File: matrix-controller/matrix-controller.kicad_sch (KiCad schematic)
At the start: 1 part

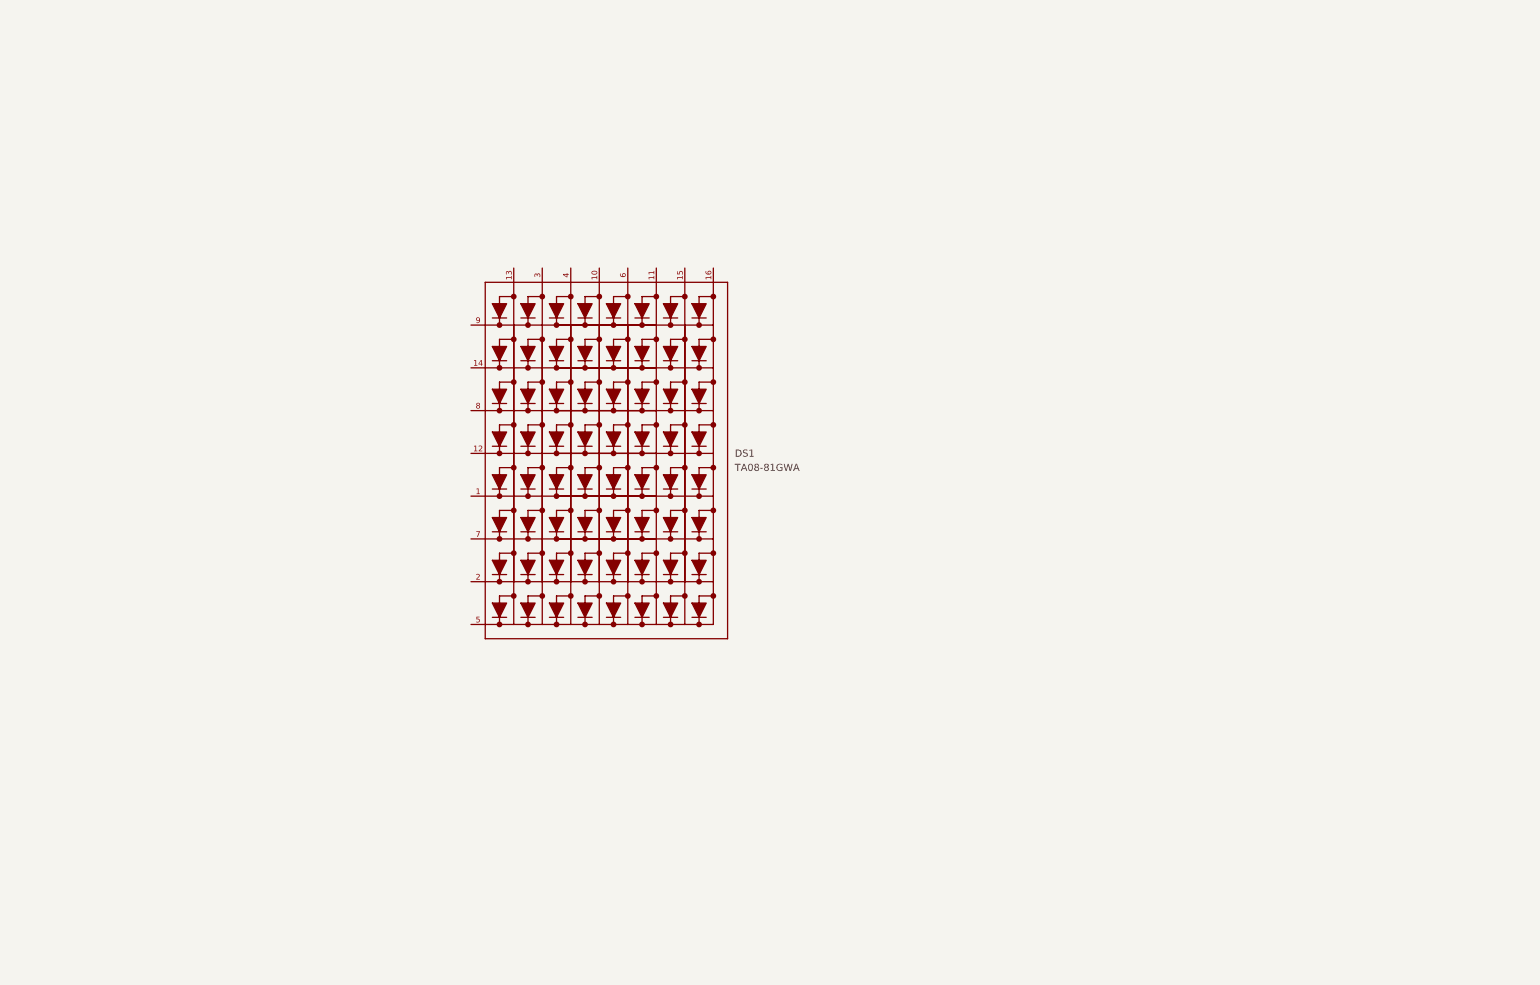
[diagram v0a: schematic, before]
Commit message: Base of the schematic is done, need to add IMU and regulator and finish the rest of the panels
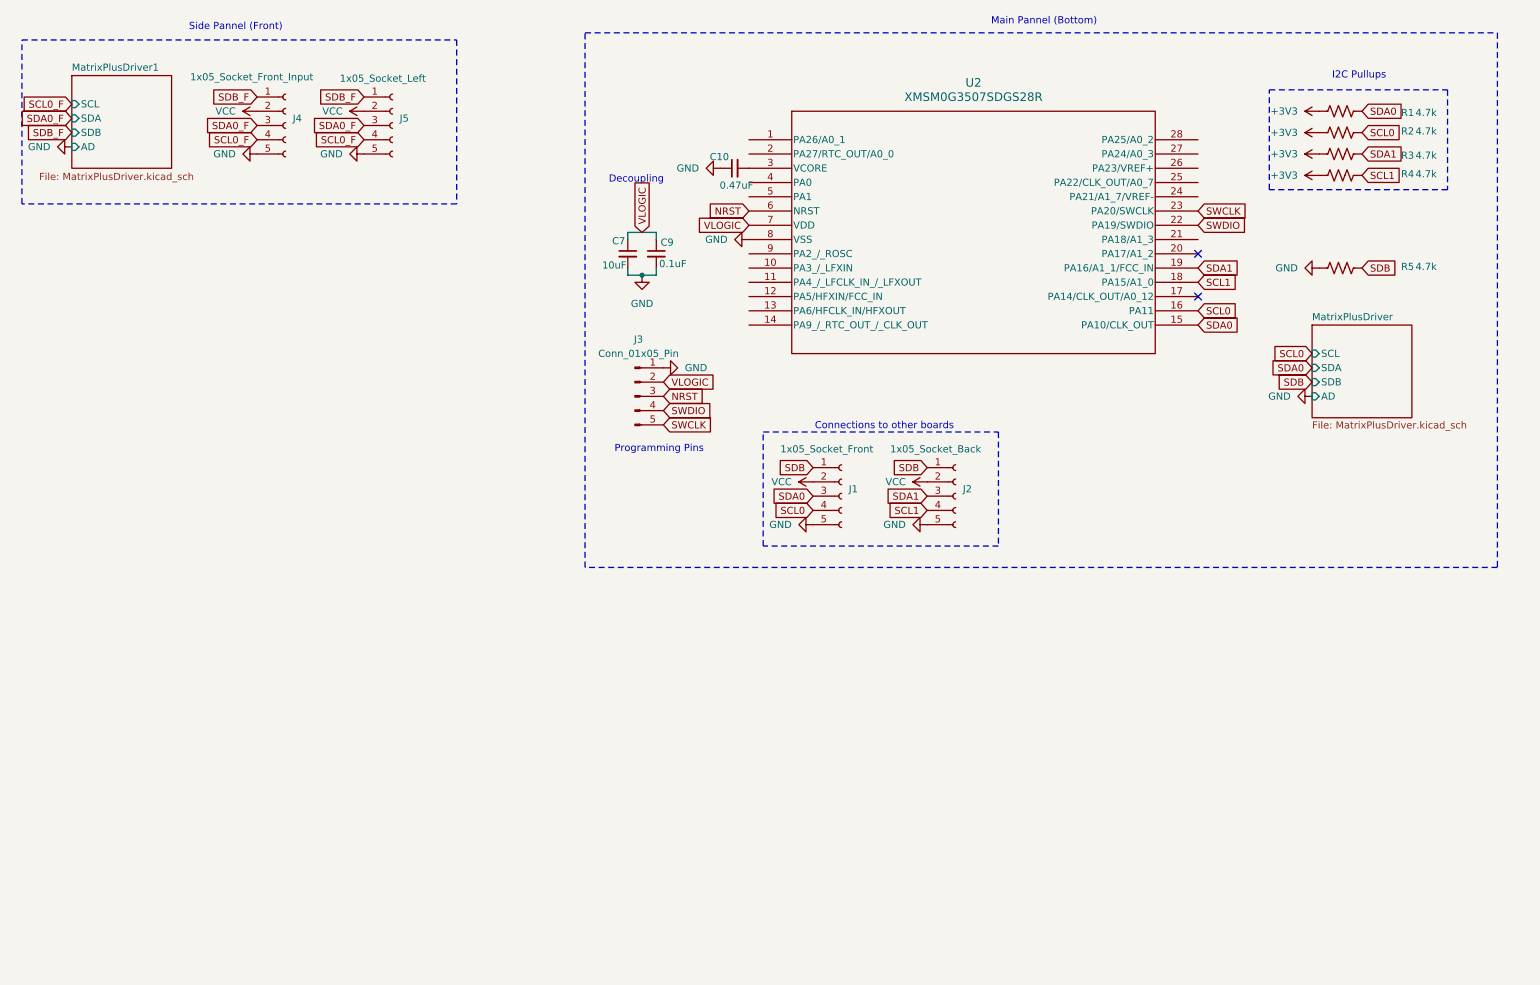
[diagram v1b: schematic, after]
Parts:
- removed DS1: TA08-81GWA, TA08-81GWA:DISPLAY_TA08-81GWA, symbol TA08-81GWA:TA08-81GWA
- added C10: 0.47uF, Capacitor_SMD:C_1206_3216Metric, symbol Device:C_Small
- added C7: 10uF, Capacitor_SMD:C_1206_3216Metric, symbol Device:C_Small
- added C9: 0.1uF, Capacitor_SMD:C_1206_3216Metric, symbol Device:C_Small
- added J1: 1x05_Socket_Front, Connector_PinSocket_2.00mm:PinSocket_1x05_P2.00mm_Vertical, symbol Connector:Conn_01x05_Socket
- added J2: 1x05_Socket_Back, Connector_PinSocket_2.00mm:PinSocket_1x05_P2.00mm_Vertical, symbol Connector:Conn_01x05_Socket
- added J3: Conn_01x05_Pin, Connector_PinSocket_2.54mm:PinSocket_1x05_P2.54mm_Vertical, symbol Connector:Conn_01x05_Pin
- added J4: 1x05_Socket_Front_Input, Connector_PinSocket_2.00mm:PinSocket_1x05_P2.00mm_Vertical, symbol Connector:Conn_01x05_Socket
- added J5: 1x05_Socket_Left, Connector_PinSocket_2.00mm:PinSocket_1x05_P2.00mm_Vertical, symbol Connector:Conn_01x05_Socket
- added R1, R2, R3, R4, R5: 4.7k, symbol Device:R_US
- added U2: XMSM0G3507SDGS28R, footprints:VSSOP28_DGS_TEX, symbol 2025-11-23_22-36-31:XMSM0G3507SDGS28R
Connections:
- new net: C10.2, U2.3 (VCORE)
- new net +3V3: R1.1, R2.1, R3.1, R4.1
- new net GND: C10.1, C7.2, C9.2, J1.5 (Pin_5), J2.5 (Pin_5), J3.1 (Pin_1), J4.5 (Pin_5), J5.5 (Pin_5), R5.1, U2.8 (VSS)
- new net NRST: J3.3 (Pin_3), U2.6 (NRST)
- new net SCL0: J1.4 (Pin_4), R2.2, U2.16 (PA11)
- new net SCL0_F: J4.4 (Pin_4), J5.4 (Pin_4)
- new net SCL1: J2.4 (Pin_4), R4.2, U2.18 (PA15/A1_0)
- new net SDA0: J1.3 (Pin_3), R1.2, U2.15 (PA10/CLK_OUT)
- new net SDA0_F: J4.3 (Pin_3), J5.3 (Pin_3)
- new net SDA1: J2.3 (Pin_3), R3.2, U2.19 (PA16/A1_1/FCC_IN)
- new net SDB: J1.1 (Pin_1), J2.1 (Pin_1), R5.2
- new net SDB_F: J4.1 (Pin_1), J5.1 (Pin_1)
- new net SWCLK: J3.5 (Pin_5), U2.23 (PA20/SWCLK)
- new net SWDIO: J3.4 (Pin_4), U2.22 (PA19/SWDIO)
- new net VCC: J1.2 (Pin_2), J2.2 (Pin_2), J4.2 (Pin_2), J5.2 (Pin_2)
- new net VLOGIC: C7.1, C9.1, J3.2 (Pin_2), U2.7 (VDD)
- no-connect marks 0 -> 2
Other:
- added sheet MatrixPlusDriver (MatrixPlusDriver.kicad_sch)
- added sheet MatrixPlusDriver1 (MatrixPlusDriver.kicad_sch)
- note added: "Connections to other boards"
- note added: "Decoupling"
- note added: "I2C Pullups"
- note added: "Main Pannel (Bottom)"
- note added: "Programming Pins"
- note added: "Side Pannel (Front)"

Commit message: Schematic of other pannels mostly completed
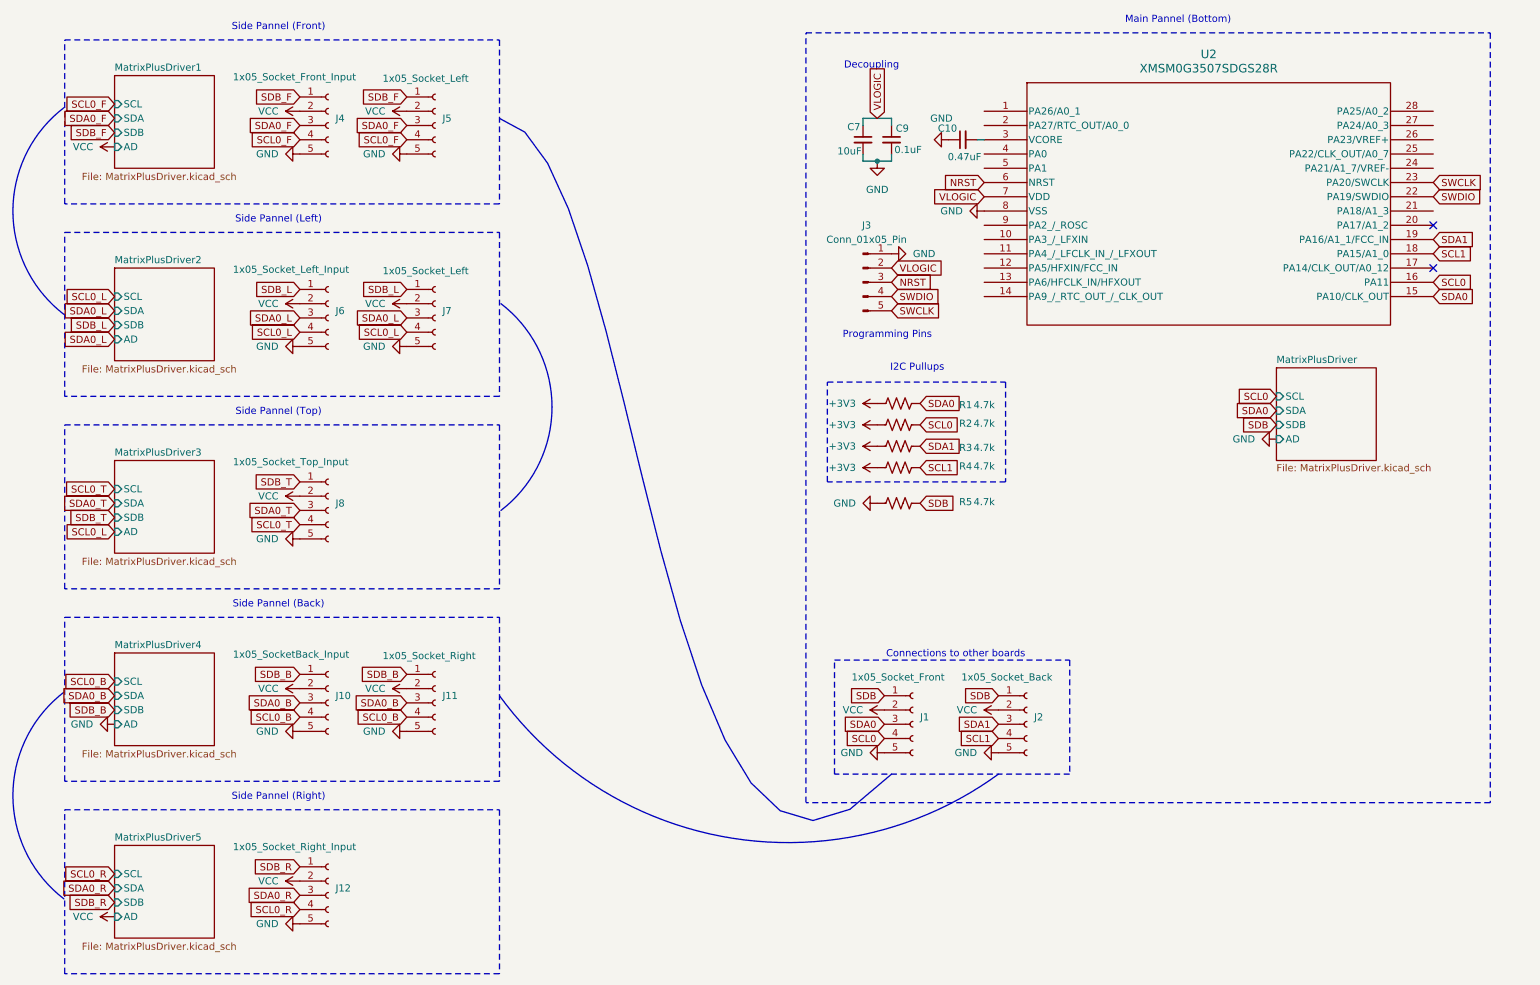
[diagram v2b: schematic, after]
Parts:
- added J10: 1x05_SocketBack_Input, Connector_PinSocket_2.00mm:PinSocket_1x05_P2.00mm_Vertical, symbol Connector:Conn_01x05_Socket
- added J11: 1x05_Socket_Right, Connector_PinSocket_2.00mm:PinSocket_1x05_P2.00mm_Vertical, symbol Connector:Conn_01x05_Socket
- added J12: 1x05_Socket_Right_Input, Connector_PinSocket_2.00mm:PinSocket_1x05_P2.00mm_Vertical, symbol Connector:Conn_01x05_Socket
- added J6: 1x05_Socket_Left_Input, Connector_PinSocket_2.00mm:PinSocket_1x05_P2.00mm_Vertical, symbol Connector:Conn_01x05_Socket
- added J7: 1x05_Socket_Left, Connector_PinSocket_2.00mm:PinSocket_1x05_P2.00mm_Vertical, symbol Connector:Conn_01x05_Socket
- added J8: 1x05_Socket_Top_Input, Connector_PinSocket_2.00mm:PinSocket_1x05_P2.00mm_Vertical, symbol Connector:Conn_01x05_Socket
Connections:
- net GND: now also J10.5 (Pin_5), J11.5 (Pin_5), J12.5 (Pin_5), J6.5 (Pin_5), J7.5 (Pin_5), J8.5 (Pin_5)
- net VCC: now also J10.2 (Pin_2), J11.2 (Pin_2), J12.2 (Pin_2), J6.2 (Pin_2), J7.2 (Pin_2), J8.2 (Pin_2)
- new net SCL0_B: J10.4 (Pin_4), J11.4 (Pin_4)
- new net SCL0_L: J6.4 (Pin_4), J7.4 (Pin_4)
- new net SCL0_R: J12.4 (Pin_4)
- new net SCL0_T: J8.4 (Pin_4)
- new net SDA0_B: J10.3 (Pin_3), J11.3 (Pin_3)
- new net SDA0_L: J6.3 (Pin_3), J7.3 (Pin_3)
- new net SDA0_R: J12.3 (Pin_3)
- new net SDA0_T: J8.3 (Pin_3)
- new net SDB_B: J10.1 (Pin_1), J11.1 (Pin_1)
- new net SDB_L: J6.1 (Pin_1), J7.1 (Pin_1)
- new net SDB_R: J12.1 (Pin_1)
- new net SDB_T: J8.1 (Pin_1)
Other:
- added sheet MatrixPlusDriver2 (MatrixPlusDriver.kicad_sch)
- added sheet MatrixPlusDriver3 (MatrixPlusDriver.kicad_sch)
- added sheet MatrixPlusDriver4 (MatrixPlusDriver.kicad_sch)
- added sheet MatrixPlusDriver5 (MatrixPlusDriver.kicad_sch)
- note added: "Side Pannel (Back)"
- note added: "Side Pannel (Left)"
- note added: "Side Pannel (Right)"
- note added: "Side Pannel (Top)"
- moved on the sheet: C10, C7, C9, J1, J2, J3, J4, J5, R1, R2, R3, R4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

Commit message: Updates to pcb. Switched to 4 wire connecions. Added IMU and usb C port footprints
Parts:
- removed J1: 1x05_Socket_Front, Connector_PinSocket_2.00mm:PinSocket_1x05_P2.00mm_Vertical, symbol Connector:Conn_01x05_Socket
- removed J10: 1x05_SocketBack_Input, Connector_PinSocket_2.00mm:PinSocket_1x05_P2.00mm_Vertical, symbol Connector:Conn_01x05_Socket
- removed J11: 1x05_Socket_Right, Connector_PinSocket_2.00mm:PinSocket_1x05_P2.00mm_Vertical, symbol Connector:Conn_01x05_Socket
- removed J12: 1x05_Socket_Right_Input, Connector_PinSocket_2.00mm:PinSocket_1x05_P2.00mm_Vertical, symbol Connector:Conn_01x05_Socket
- removed J2: 1x05_Socket_Back, Connector_PinSocket_2.00mm:PinSocket_1x05_P2.00mm_Vertical, symbol Connector:Conn_01x05_Socket
- removed J4: 1x05_Socket_Front_Input, Connector_PinSocket_2.00mm:PinSocket_1x05_P2.00mm_Vertical, symbol Connector:Conn_01x05_Socket
- removed J5, J7: 1x05_Socket_Left, Connector_PinSocket_2.00mm:PinSocket_1x05_P2.00mm_Vertical, symbol Connector:Conn_01x05_Socket
- removed J6: 1x05_Socket_Left_Input, Connector_PinSocket_2.00mm:PinSocket_1x05_P2.00mm_Vertical, symbol Connector:Conn_01x05_Socket
- removed J8: 1x05_Socket_Top_Input, Connector_PinSocket_2.00mm:PinSocket_1x05_P2.00mm_Vertical, symbol Connector:Conn_01x05_Socket
- added J1: 1x04_Socket_Front, Connector_Wire:SolderWire-0.1sqmm_1x04_P3.6mm_D0.4mm_OD1mm, symbol Connector:Conn_01x04_Pin
- added J11: 1x05_Socket_Right_Input, Connector_Wire:SolderWire-0.1sqmm_1x04_P3.6mm_D0.4mm_OD1mm, symbol Connector:Conn_01x04_Pin
- added J13: 1x05_Socket_Right, Connector_Wire:SolderWire-0.1sqmm_1x04_P3.6mm_D0.4mm_OD1mm, symbol Connector:Conn_01x04_Pin
- added J2: 1x04_Socket_Back, Connector_Wire:SolderWire-0.1sqmm_1x04_P3.6mm_D0.4mm_OD1mm, symbol Connector:Conn_01x04_Pin
- added J4: 1x04_Socket_Left_Input, Connector_Wire:SolderWire-0.1sqmm_1x04_P3.6mm_D0.4mm_OD1mm, symbol Connector:Conn_01x04_Pin
- added J5: 1x04_Socket_Top, Connector_Wire:SolderWire-0.1sqmm_1x04_P3.6mm_D0.4mm_OD1mm, symbol Connector:Conn_01x04_Pin
- added J6: 1x04_Socket_Front_Input, Connector_Wire:SolderWire-0.1sqmm_1x04_P3.6mm_D0.4mm_OD1mm, symbol Connector:Conn_01x04_Pin
- added J7: 1x04_Socket_Left, Connector_Wire:SolderWire-0.1sqmm_1x04_P3.6mm_D0.4mm_OD1mm, symbol Connector:Conn_01x04_Pin
- added J8: 1x05_SocketBack_Input, Connector_Wire:SolderWire-0.1sqmm_1x04_P3.6mm_D0.4mm_OD1mm, symbol Connector:Conn_01x04_Pin
- added J9: 1x04_Socket_Top_Input, Connector_Wire:SolderWire-0.1sqmm_1x04_P3.6mm_D0.4mm_OD1mm, symbol Connector:Conn_01x04_Pin
- added U1: ICM-42370-P, .pretty:PQFN50P250X300X81-14N, symbol ICM-42370-P:ICM-42370-P
- added USBC: UJC-H-G-SMT-2-P6-TR, .pretty:UJCHGSMT2P6TR, symbol UJC-H-G-SMT-2-P6-TR:UJC-H-G-SMT-2-P6-TR
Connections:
- net GND: now also J1.1 (Pin_1), J11.1 (Pin_1), J13.1 (Pin_1), J2.1 (Pin_1), J4.1 (Pin_1), J5.1 (Pin_1), J6.1 (Pin_1), J7.1 (Pin_1), J8.1 (Pin_1), J9.1 (Pin_1), U1.6 (GND), USBC.A12 (GND_1), USBC.B12 (GND_2)
- net SCL0: now also J1.2 (Pin_2)
- net SCL0_B: now also J13.2 (Pin_2), J8.2 (Pin_2)
- net SCL0_F: now also J6.2 (Pin_2), J7.2 (Pin_2)
- net SCL0_L: now also J4.2 (Pin_2), J5.2 (Pin_2)
- net SCL0_R: now also J11.2 (Pin_2)
- net SCL0_T: now also J9.2 (Pin_2)
- net SCL1: now also J2.2 (Pin_2)
- net SDA0: now also J1.3 (Pin_3)
- net SDA0_B: now also J13.3 (Pin_3), J8.3 (Pin_3)
- net SDA0_F: now also J6.3 (Pin_3), J7.3 (Pin_3)
- net SDA0_L: now also J4.3 (Pin_3), J5.3 (Pin_3)
- net SDA0_R: now also J11.3 (Pin_3)
- net SDA0_T: now also J9.3 (Pin_3)
- net SDA1: now also J2.3 (Pin_3)
- net VCC: now also J1.4 (Pin_4), J11.4 (Pin_4), J13.4 (Pin_4), J2.4 (Pin_4), J4.4 (Pin_4), J5.4 (Pin_4), J6.4 (Pin_4), J7.4 (Pin_4), J8.4 (Pin_4), J9.4 (Pin_4)
- net VLOGIC renamed +3.3V
- new net: U1.10 (RESV), U1.11 (RESV), U1.2 (RESV), U1.3 (RESV), U1.7 (RESV)
- new net +5V: USBC.A9 (VBUS_1), USBC.B9 (VBUS_2)
- no-connect marks 2 -> 7
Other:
- removed sheet MatrixPlusDriver
